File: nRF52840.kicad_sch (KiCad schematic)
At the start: 19 parts, among them J3 JTAG_TC2030, J4 RGB, Q2 2N7002, Q3 AO3407, SW29 RESET, U4 MS88SF3

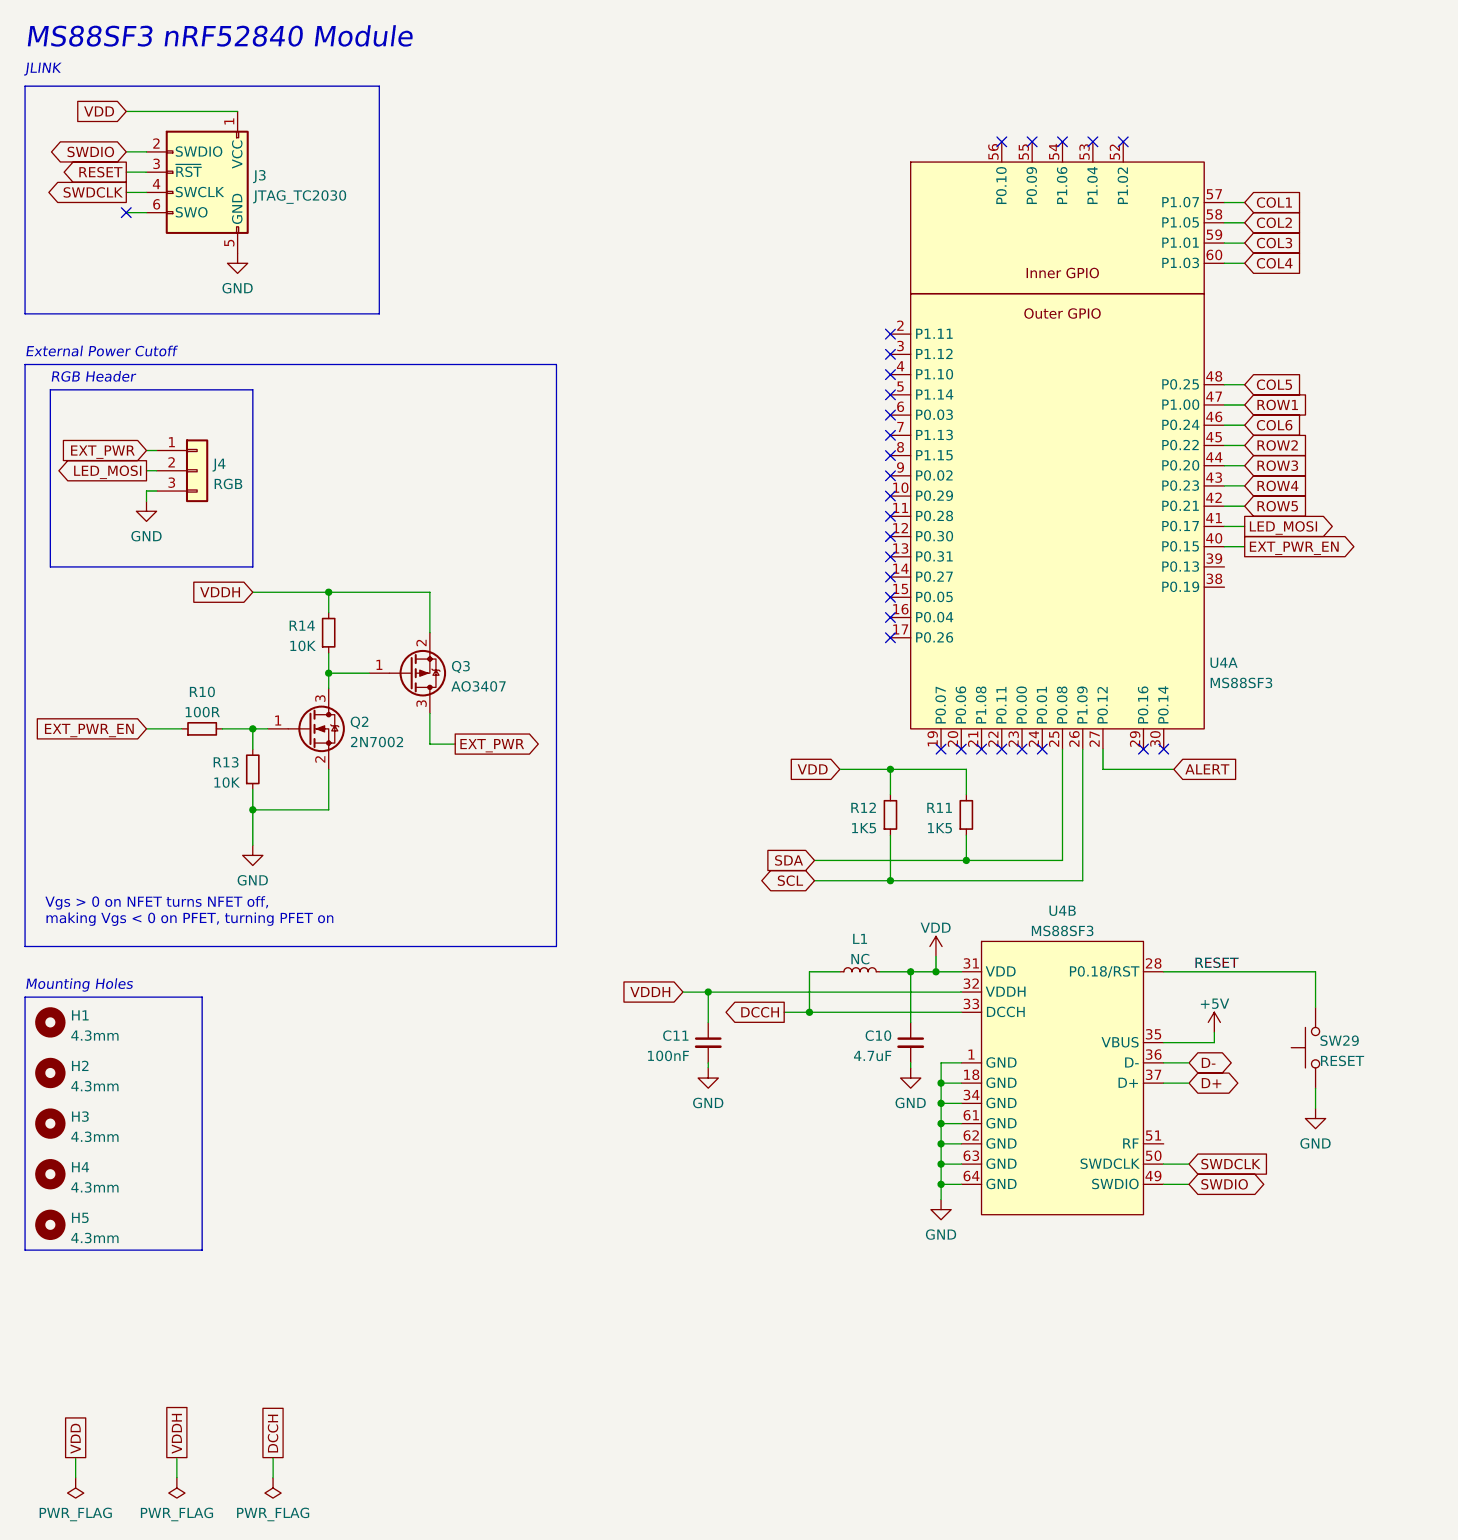
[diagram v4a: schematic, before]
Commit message: feat(pcb): Version 0.2.2
- Update MS88SF3 footprint
- Create thumb cluster silksscreen
- Separate NTPH and PTH drill files
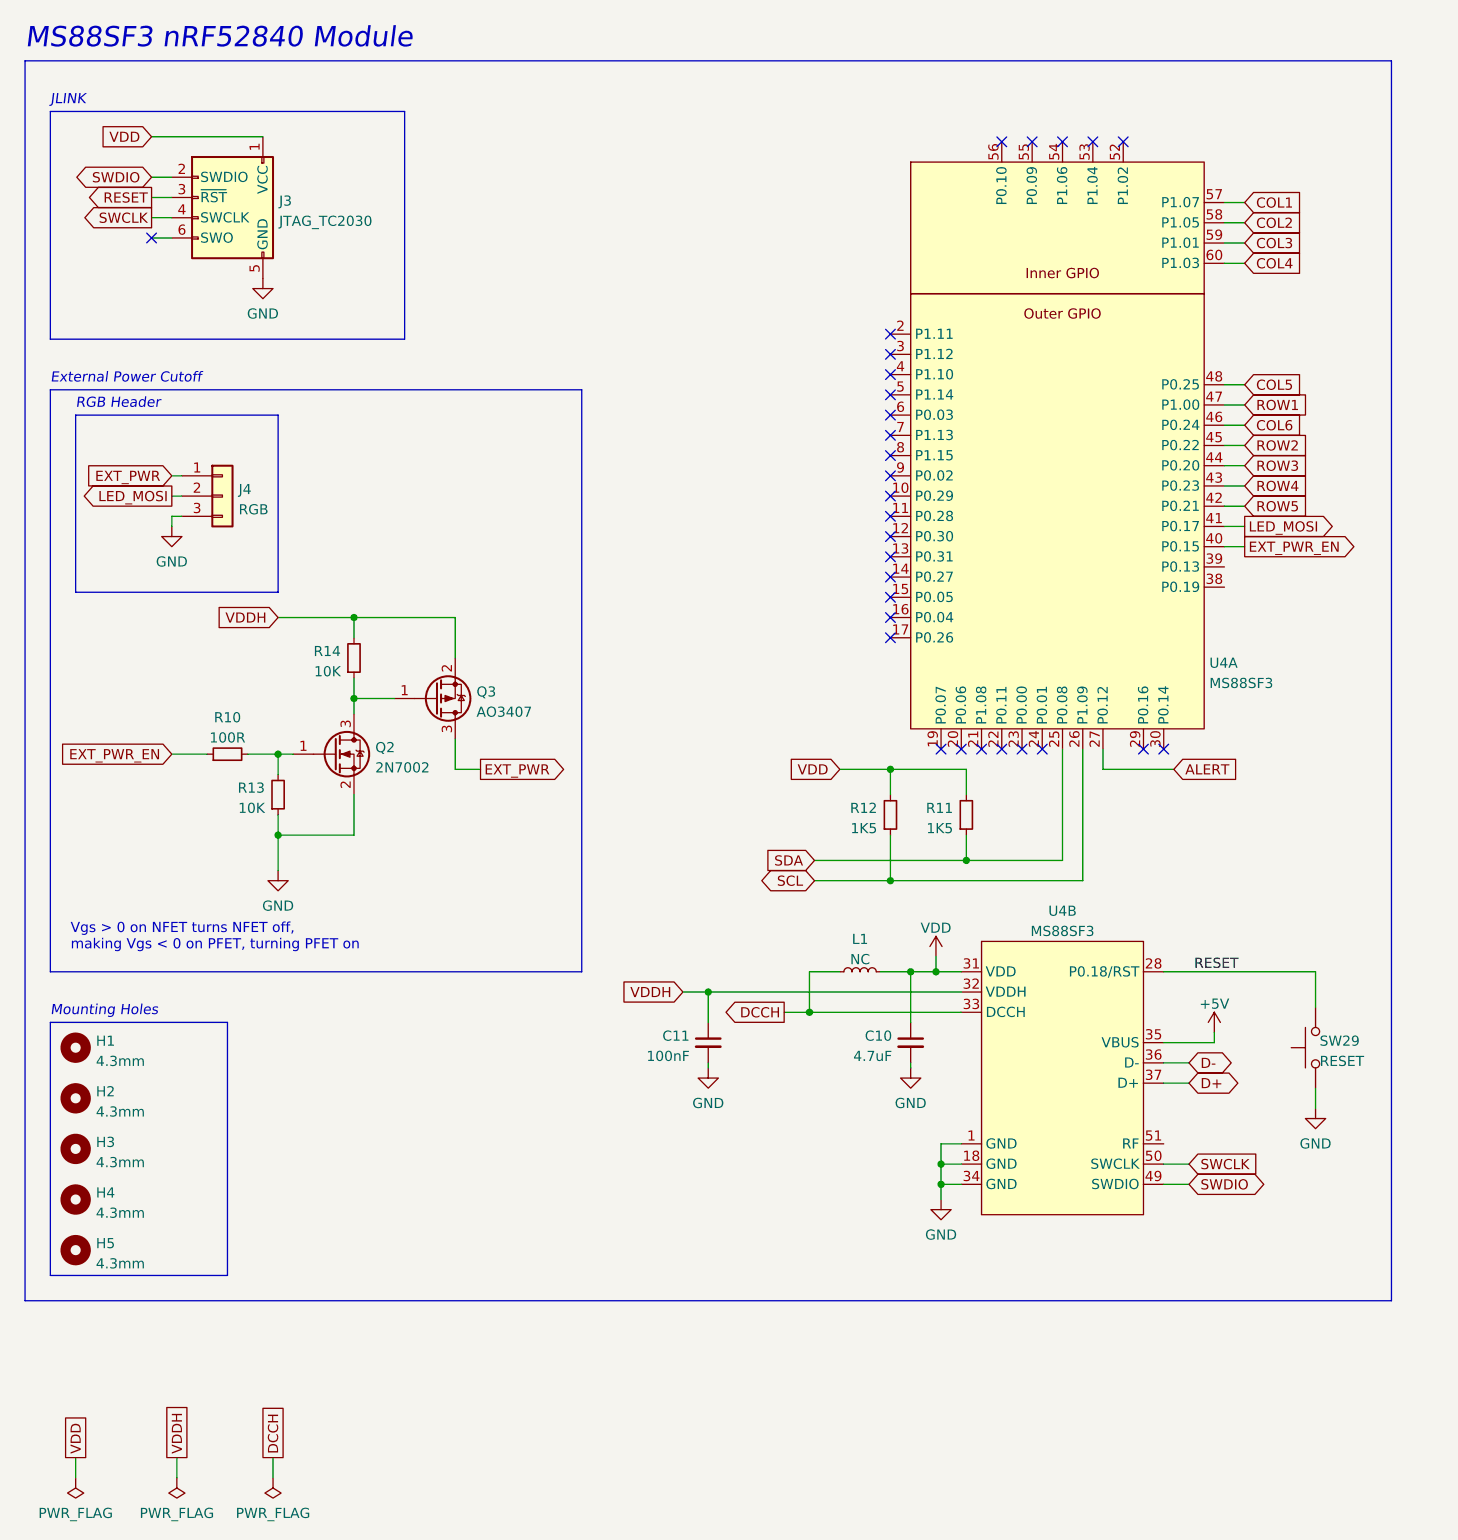
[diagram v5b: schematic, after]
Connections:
- net GND: no longer U4.61 (GND), U4.62 (GND), U4.63 (GND), U4.64 (GND)
- net SWDCLK renamed SWCLK
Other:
- moved on the sheet: H1, H2, H3, H4, H5, J3, J4, Q2, Q3, R10, R13, R14

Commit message: fix(pcb): Finalize part selection
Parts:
- C11: value 100nF -> (none); footprint Capacitor_SMD:C_0402_1005Metric -> (none)
- L1: value NC -> (none); footprint Inductor_SMD:L_0402_1005Metric -> Inductor_SMD:L_0603_1608Metric
- U4: footprint Conejo:MS88SF3 -> Conejo:MS88SF3_PeteJohanson
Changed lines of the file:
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@@
       (effects (font (size 1.27 1.27)) (justify left))
     )
-    (property "Value" "100nF" (id 1) (at 96.1009 143.9485 0)
-      (effects (font (size 1.27 1.27)) (justify left))
-    )
-    (property "Footprint" "Capacitor_SMD:C_0402_1005Metric" (id 2) (at 98.425 142.24 0)
+    (property "Value" "" (id 1) (at 96.1009 143.9485 0)
+      (effects (font (size 1.27 1.27)) (justify left))
+    )
+    (property "Footprint" "" (id 2) (at 98.425 142.24 0)
       (effects (font (size 1.27 1.27)) hide)
     )
@@
     (property "Reference" "U4" (id 0) (at 142.875 125.7331 0))
     (property "Value" "MS88SF3" (id 1) (at 142.875 128.27 0))
-    (property "Footprint" "Conejo:MS88SF3" (id 2) (at 170.815 179.07 0)
+    (property "Footprint" "Conejo:MS88SF3_PeteJohanson" (id 2) (at 170.815 179.07 0)
       (effects (font (size 1.27 1.27)) hide)
     )
@@
       (effects (font (size 1.27 1.27)) (justify left))
     )
-    (property "Footprint" "Conejo:MS88SF3" (id 2) (at 170.815 100.33 0)
+    (property "Footprint" "Conejo:MS88SF3_PeteJohanson" (id 2) (at 170.815 100.33 0)
       (effects (font (size 1.27 1.27)) hide)
     )
@@
     (in_bom yes) (on_board yes) (fields_autoplaced)
     (property "Reference" "L1" (id 0) (at 117.475 129.2692 90))
-    (property "Value" "NC" (id 1) (at 117.475 131.8061 90))
-    (property "Footprint" "Inductor_SMD:L_0402_1005Metric" (id 2) (at 117.475 133.35 0)
-      (effects (font (size 1.27 1.27)) hide)
-    )
+    (property "Value" "" (id 1) (at 117.475 131.8061 90))
+    (property "Footprint" "Inductor_SMD:L_0603_1608Metric" (id 2) (at 117.475 133.35 0)
+      (effects (font (size 1.27 1.27)) hide)
+    )

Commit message: fix(schematic): Fix inductor value in DCCH LC filter
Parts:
- C11: value (none) -> 4.7uF; footprint (none) -> Capacitor_SMD:C_0402_1005Metric
- L1: value (none) -> 10uH
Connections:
- no-connect marks 30 -> 31
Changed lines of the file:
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@@
   (no_connect (at 121.285 88.9))
   (no_connect (at 121.285 91.44))
+  (no_connect (at 163.195 85.09))
   (no_connect (at 127.635 105.41))
   (no_connect (at 28.575 41.275))
@@
       (effects (font (size 1.27 1.27)) (justify left))
     )
-    (property "Value" "" (id 1) (at 96.1009 143.9485 0)
-      (effects (font (size 1.27 1.27)) (justify left))
-    )
-    (property "Footprint" "" (id 2) (at 98.425 142.24 0)
+    (property "Value" "4.7uF" (id 1) (at 96.1009 143.9485 0)
+      (effects (font (size 1.27 1.27)) (justify left))
+    )
+    (property "Footprint" "Capacitor_SMD:C_0402_1005Metric" (id 2) (at 98.425 142.24 0)
       (effects (font (size 1.27 1.27)) hide)
     )
@@
     (in_bom yes) (on_board yes) (fields_autoplaced)
     (property "Reference" "L1" (id 0) (at 117.475 129.2692 90))
-    (property "Value" "" (id 1) (at 117.475 131.8061 90))
+    (property "Value" "10uH" (id 1) (at 117.475 131.8061 90))
     (property "Footprint" "Inductor_SMD:L_0603_1608Metric" (id 2) (at 117.475 133.35 0)
       (effects (font (size 1.27 1.27)) hide)

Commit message: feat(pcb): Version 0.3
- Move components entirely to back copper :tada:
- Update silkscreen legibility to enhance ease of component placement
- Fix I2C pullup resistors
  - Replace incorrect value of 1K5 with 5K1
  - Update footprint to 0603_1608 to fit VDD traces underneath, compared to original 0402_1005 footprint
- Increase text width on RESET button, POWER Switch, and CHG LED
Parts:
- added C10: 4u7F, Capacitor_SMD:C_0402_1005Metric, symbol Device:C_Small
- C8: renamed from C10; value 4.7uF -> 4u7F
- C9: renamed from C11; value 4.7uF -> 4u7F
- R11, R12: value 1K5 -> 5K1; footprint Resistor_SMD:R_0402_1005Metric -> Resistor_SMD:R_0603_1608Metric
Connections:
- net +5V: now also C10.1
- net ALERT: now also U4.17 (P0.26); no longer U4.27 (P0.12)
- net GND: now also C10.2
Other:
- moved on the sheet: SW29
